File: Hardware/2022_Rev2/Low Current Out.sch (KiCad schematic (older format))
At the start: 72 parts

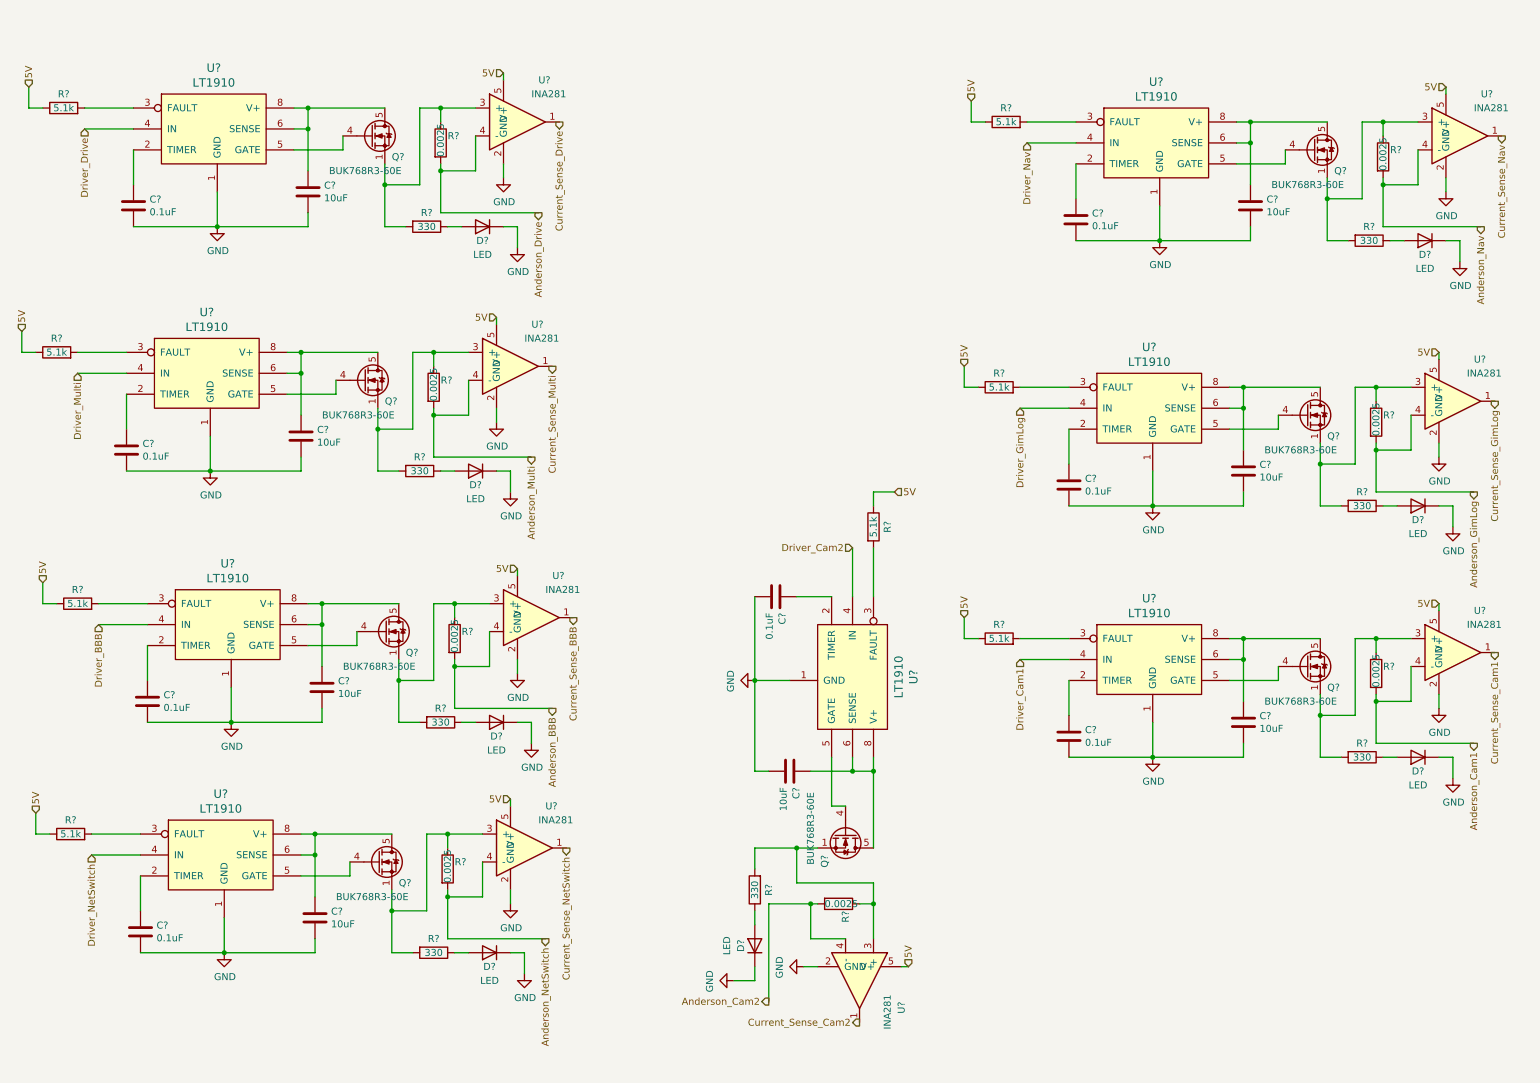
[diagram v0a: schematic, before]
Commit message: assigning footprints pt.1
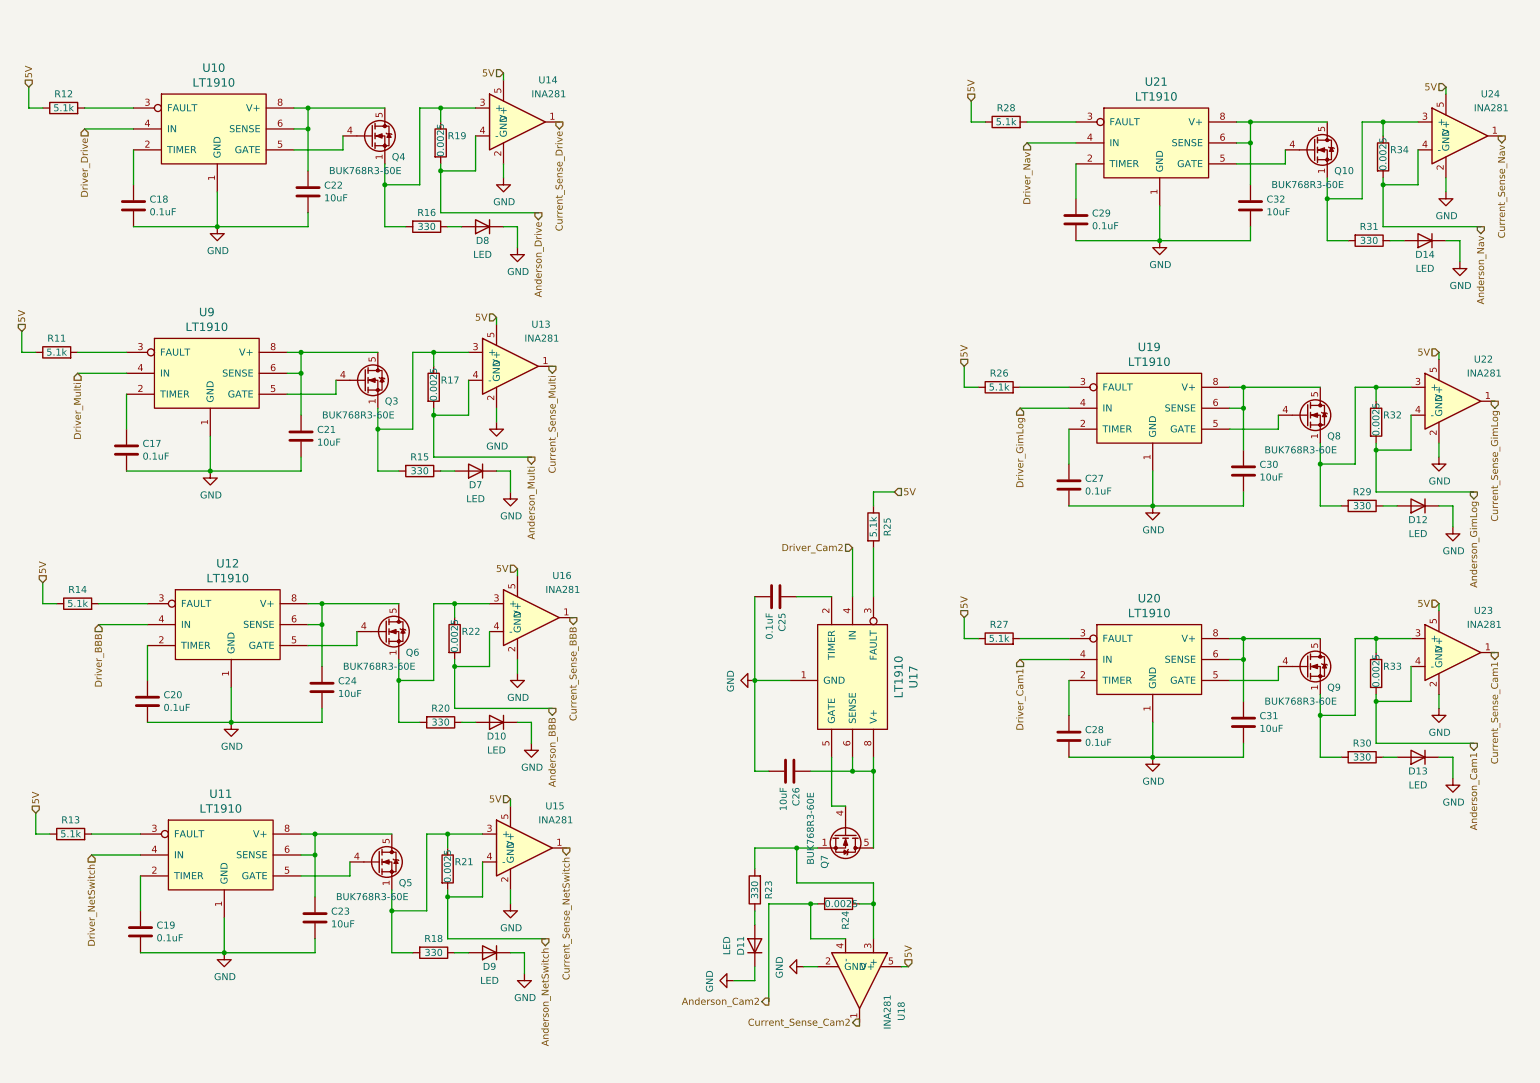
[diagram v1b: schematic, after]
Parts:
- C17, C18, C19, C20, C21, C22, C23, C24, C25, C26, C27, C28, C29, C30, C31, C32: renamed from C?; footprint (none) -> Capacitor_SMD:C_0603_1608Metric_Pad1.08x0.95mm_HandSolder
- D10, D11, D12, D13, D14, D7, D8, D9: renamed from D?; footprint (none) -> Diode_SMD:D_0603_1608Metric_Pad1.05x0.95mm_HandSolder
- gave numbers to parts that had none: 48

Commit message: Finished footprint signatures and started schematic
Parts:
- R11, R12, R13, R14, R15, R16, R18, R20, R23, R25, R26, R27, R28, R29, R30, R31: footprint (none) -> Resistor_SMD:R_0603_1608Metric_Pad0.98x0.95mm_HandSolder
- R17, R19, R21, R22, R24, R32, R33, R34: footprint (none) -> Resistor_SMD:R_2512_6332Metric_Pad1.40x3.35mm_HandSolder
- U10, U11, U12, U17, U19, U20, U21, U9: footprint (none) -> Package_SO:SOIC-8_3.9x4.9mm_P1.27mm
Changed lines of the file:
@@
 F 0 "R14" V 1000 4650 50  0000 C CNN
 F 1 "5.1k" V 900 4650 50  0000 C CNN
-F 2 "" V 830 4650 50  0001 C CNN
+F 2 "Resistor_SMD:R_0603_1608Metric_Pad0.98x0.95mm_HandSolder" V 830 4650 50  0001 C CNN
 F 3 "~" H 900 4650 50  0001 C CNN
 	1    900  4650
@@
 F 0 "U12" H 1975 5737 60  0000 C CNN
 F 1 "LT1910" H 1975 5631 60  0000 C CNN
-F 2 "" H 1600 5050 60  0001 C CNN
+F 2 "Package_SO:SOIC-8_3.9x4.9mm_P1.27mm" H 1600 5050 60  0001 C CNN
 F 3 "" H 1600 5050 60  0001 C CNN
 	1    1600 5050
@@
 F 0 "R20" V 3400 5500 50  0000 C CNN
 F 1 "330" V 3500 5500 50  0000 C CNN
-F 2 "" V 3430 5500 50  0001 C CNN
+F 2 "Resistor_SMD:R_0603_1608Metric_Pad0.98x0.95mm_HandSolder" V 3430 5500 50  0001 C CNN
 F 3 "~" H 3500 5500 50  0001 C CNN
 	1    3500 5500
@@
 F 0 "R22" H 3650 4950 50  0000 L CNN
 F 1 "0.0025" V 3600 4800 50  0000 L CNN
-F 2 "" V 3530 4900 50  0001 C CNN
+F 2 "Resistor_SMD:R_2512_6332Metric_Pad1.40x3.35mm_HandSolder" V 3530 4900 50  0001 C CNN
 F 3 "~" H 3600 4900 50  0001 C CNN
 	1    3600 4900
@@
 F 0 "R11" V 850 2850 50  0000 C CNN
 F 1 "5.1k" V 750 2850 50  0000 C CNN
-F 2 "" V 680 2850 50  0001 C CNN
+F 2 "Resistor_SMD:R_0603_1608Metric_Pad0.98x0.95mm_HandSolder" V 680 2850 50  0001 C CNN
 F 3 "~" H 750 2850 50  0001 C CNN
 	1    750  2850
@@
 F 0 "U9" H 1825 3937 60  0000 C CNN
 F 1 "LT1910" H 1825 3831 60  0000 C CNN
-F 2 "" H 1450 3250 60  0001 C CNN
+F 2 "Package_SO:SOIC-8_3.9x4.9mm_P1.27mm" H 1450 3250 60  0001 C CNN
 F 3 "" H 1450 3250 60  0001 C CNN
 	1    1450 3250
@@
 F 0 "R15" V 3250 3700 50  0000 C CNN
 F 1 "330" V 3350 3700 50  0000 C CNN
-F 2 "" V 3280 3700 50  0001 C CNN
+F 2 "Resistor_SMD:R_0603_1608Metric_Pad0.98x0.95mm_HandSolder" V 3280 3700 50  0001 C CNN
 F 3 "~" H 3350 3700 50  0001 C CNN
 	1    3350 3700
@@
 F 0 "R17" H 3500 3150 50  0000 L CNN
 F 1 "0.0025" V 3450 3000 50  0000 L CNN
-F 2 "" V 3380 3100 50  0001 C CNN
+F 2 "Resistor_SMD:R_2512_6332Metric_Pad1.40x3.35mm_HandSolder" V 3380 3100 50  0001 C CNN
 F 3 "~" H 3450 3100 50  0001 C CNN
 	1    3450 3100
@@
 F 0 "R12" V 900 1100 50  0000 C CNN
 F 1 "5.1k" V 800 1100 50  0000 C CNN
-F 2 "" V 730 1100 50  0001 C CNN
+F 2 "Resistor_SMD:R_0603_1608Metric_Pad0.98x0.95mm_HandSolder" V 730 1100 50  0001 C CNN
 F 3 "~" H 800 1100 50  0001 C CNN
 	1    800  1100
@@
 F 0 "U10" H 1875 2187 60  0000 C CNN
 F 1 "LT1910" H 1875 2081 60  0000 C CNN
-F 2 "" H 1500 1500 60  0001 C CNN
+F 2 "Package_SO:SOIC-8_3.9x4.9mm_P1.27mm" H 1500 1500 60  0001 C CNN
 F 3 "" H 1500 1500 60  0001 C CNN
 	1    1500 1500
@@
 F 0 "R16" V 3300 1950 50  0000 C CNN
 F 1 "330" V 3400 1950 50  0000 C CNN
-F 2 "" V 3330 1950 50  0001 C CNN
+F 2 "Resistor_SMD:R_0603_1608Metric_Pad0.98x0.95mm_HandSolder" V 3330 1950 50  0001 C CNN
 F 3 "~" H 3400 1950 50  0001 C CNN
 	1    3400 1950
@@
 F 0 "R19" H 3550 1400 50  0000 L CNN
 F 1 "0.0025" V 3500 1250 50  0000 L CNN
-F 2 "" V 3430 1350 50  0001 C CNN
+F 2 "Resistor_SMD:R_2512_6332Metric_Pad1.40x3.35mm_HandSolder" V 3430 1350 50  0001 C CNN
 F 3 "~" H 3500 1350 50  0001 C CNN
 	1    3500 1350
@@
 F 0 "R28" V 7650 1200 50  0000 C CNN
 F 1 "5.1k" V 7550 1200 50  0000 C CNN
-F 2 "" V 7480 1200 50  0001 C CNN
+F 2 "Resistor_SMD:R_0603_1608Metric_Pad0.98x0.95mm_HandSolder" V 7480 1200 50  0001 C CNN
 F 3 "~" H 7550 1200 50  0001 C CNN
 	1    7550 1200
@@
 F 0 "U21" H 8625 2287 60  0000 C CNN
 F 1 "LT1910" H 8625 2181 60  0000 C CNN
-F 2 "" H 8250 1600 60  0001 C CNN
+F 2 "Package_SO:SOIC-8_3.9x4.9mm_P1.27mm" H 8250 1600 60  0001 C CNN
 F 3 "" H 8250 1600 60  0001 C CNN
 	1    8250 1600
@@
 F 0 "R31" V 10050 2050 50  0000 C CNN
 F 1 "330" V 10150 2050 50  0000 C CNN
-F 2 "" V 10080 2050 50  0001 C CNN
+F 2 "Resistor_SMD:R_0603_1608Metric_Pad0.98x0.95mm_HandSolder" V 10080 2050 50  0001 C CNN
 F 3 "~" H 10150 2050 50  0001 C CNN
 	1    10150 2050
@@
 F 0 "R34" H 10300 1500 50  0000 L CNN
 F 1 "0.0025" V 10250 1350 50  0000 L CNN
-F 2 "" V 10180 1450 50  0001 C CNN
+F 2 "Resistor_SMD:R_2512_6332Metric_Pad1.40x3.35mm_HandSolder" V 10180 1450 50  0001 C CNN
 F 3 "~" H 10250 1450 50  0001 C CNN
 	1    10250 1450
@@
 F 0 "R26" V 7600 3100 50  0000 C CNN
 F 1 "5.1k" V 7500 3100 50  0000 C CNN
-F 2 "" V 7430 3100 50  0001 C CNN
+F 2 "Resistor_SMD:R_0603_1608Metric_Pad0.98x0.95mm_HandSolder" V 7430 3100 50  0001 C CNN
 F 3 "~" H 7500 3100 50  0001 C CNN
 	1    7500 3100
@@
 F 0 "U19" H 8575 4187 60  0000 C CNN
 F 1 "LT1910" H 8575 4081 60  0000 C CNN
-F 2 "" H 8200 3500 60  0001 C CNN
+F 2 "Package_SO:SOIC-8_3.9x4.9mm_P1.27mm" H 8200 3500 60  0001 C CNN
 F 3 "" H 8200 3500 60  0001 C CNN
 	1    8200 3500
@@
 F 0 "R29" V 10000 3950 50  0000 C CNN
 F 1 "330" V 10100 3950 50  0000 C CNN
-F 2 "" V 10030 3950 50  0001 C CNN
+F 2 "Resistor_SMD:R_0603_1608Metric_Pad0.98x0.95mm_HandSolder" V 10030 3950 50  0001 C CNN
 F 3 "~" H 10100 3950 50  0001 C CNN
 	1    10100 3950
@@
 F 0 "R32" H 10250 3400 50  0000 L CNN
 F 1 "0.0025" V 10200 3250 50  0000 L CNN
-F 2 "" V 10130 3350 50  0001 C CNN
+F 2 "Resistor_SMD:R_2512_6332Metric_Pad1.40x3.35mm_HandSolder" V 10130 3350 50  0001 C CNN
 F 3 "~" H 10200 3350 50  0001 C CNN
 	1    10200 3350
@@
 F 0 "R27" V 7600 4900 50  0000 C CNN
 F 1 "5.1k" V 7500 4900 50  0000 C CNN
-F 2 "" V 7430 4900 50  0001 C CNN
+F 2 "Resistor_SMD:R_0603_1608Metric_Pad0.98x0.95mm_HandSolder" V 7430 4900 50  0001 C CNN
 F 3 "~" H 7500 4900 50  0001 C CNN
 	1    7500 4900
@@
 F 0 "U20" H 8575 5987 60  0000 C CNN
 F 1 "LT1910" H 8575 5881 60  0000 C CNN
-F 2 "" H 8200 5300 60  0001 C CNN
+F 2 "Package_SO:SOIC-8_3.9x4.9mm_P1.27mm" H 8200 5300 60  0001 C CNN
 F 3 "" H 8200 5300 60  0001 C CNN
 	1    8200 5300
@@
 F 0 "R30" V 10000 5750 50  0000 C CNN
 F 1 "330" V 10100 5750 50  0000 C CNN
-F 2 "" V 10030 5750 50  0001 C CNN
+F 2 "Resistor_SMD:R_0603_1608Metric_Pad0.98x0.95mm_HandSolder" V 10030 5750 50  0001 C CNN
 F 3 "~" H 10100 5750 50  0001 C CNN
 	1    10100 5750
@@
 F 0 "R33" H 10250 5200 50  0000 L CNN
 F 1 "0.0025" V 10200 5050 50  0000 L CNN
-F 2 "" V 10130 5150 50  0001 C CNN
+F 2 "Resistor_SMD:R_2512_6332Metric_Pad1.40x3.35mm_HandSolder" V 10130 5150 50  0001 C CNN
 F 3 "~" H 10200 5150 50  0001 C CNN
 	1    10200 5150
@@
 F 0 "R13" V 950 6300 50  0000 C CNN
 F 1 "5.1k" V 850 6300 50  0000 C CNN
-F 2 "" V 780 6300 50  0001 C CNN
+F 2 "Resistor_SMD:R_0603_1608Metric_Pad0.98x0.95mm_HandSolder" V 780 6300 50  0001 C CNN
 F 3 "~" H 850 6300 50  0001 C CNN
 	1    850  6300
@@
 F 0 "U11" H 1925 7387 60  0000 C CNN
 F 1 "LT1910" H 1925 7281 60  0000 C CNN
-F 2 "" H 1550 6700 60  0001 C CNN
+F 2 "Package_SO:SOIC-8_3.9x4.9mm_P1.27mm" H 1550 6700 60  0001 C CNN
 F 3 "" H 1550 6700 60  0001 C CNN
 	1    1550 6700
@@
 F 0 "R18" V 3350 7150 50  0000 C CNN
 F 1 "330" V 3450 7150 50  0000 C CNN
-F 2 "" V 3380 7150 50  0001 C CNN
+F 2 "Resistor_SMD:R_0603_1608Metric_Pad0.98x0.95mm_HandSolder" V 3380 7150 50  0001 C CNN
 F 3 "~" H 3450 7150 50  0001 C CNN
 	1    3450 7150
@@
 F 0 "R21" H 3600 6600 50  0000 L CNN
 F 1 "0.0025" V 3550 6450 50  0000 L CNN
-F 2 "" V 3480 6550 50  0001 C CNN
+F 2 "Resistor_SMD:R_2512_6332Metric_Pad1.40x3.35mm_HandSolder" V 3480 6550 50  0001 C CNN
 F 3 "~" H 3550 6550 50  0001 C CNN
 	1    3550 6550
@@
 F 0 "R25" V 6700 4100 50  0000 C CNN
 F 1 "5.1k" V 6600 4100 50  0000 C CNN
-F 2 "" V 6530 4100 50  0001 C CNN
+F 2 "Resistor_SMD:R_0603_1608Metric_Pad0.98x0.95mm_HandSolder" V 6530 4100 50  0001 C CNN
 F 3 "~" H 6600 4100 50  0001 C CNN
 	1    6600 4100
@@
 F 0 "U17" H 6575 5487 60  0000 C CNN
 F 1 "LT1910" H 6575 5381 60  0000 C CNN
-F 2 "" H 6200 4800 60  0001 C CNN
+F 2 "Package_SO:SOIC-8_3.9x4.9mm_P1.27mm" H 6200 4800 60  0001 C CNN
 F 3 "" H 6200 4800 60  0001 C CNN
 	1    6200 4800
@@
 F 0 "R23" V 5650 6700 50  0000 C CNN
 F 1 "330" V 5750 6700 50  0000 C CNN
-F 2 "" V 5680 6700 50  0001 C CNN
+F 2 "Resistor_SMD:R_0603_1608Metric_Pad0.98x0.95mm_HandSolder" V 5680 6700 50  0001 C CNN
 F 3 "~" H 5750 6700 50  0001 C CNN
 	1    5750 6700
@@
 F 0 "R24" H 6400 6850 50  0000 L CNN
 F 1 "0.0025" V 6350 6700 50  0000 L CNN
-F 2 "" V 6280 6800 50  0001 C CNN
+F 2 "Resistor_SMD:R_2512_6332Metric_Pad1.40x3.35mm_HandSolder" V 6280 6800 50  0001 C CNN
 F 3 "~" H 6350 6800 50  0001 C CNN
 	1    6350 6800

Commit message: Lots of Changes
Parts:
- added C?: 0.1uF, Capacitor_SMD:C_0603_1608Metric_Pad1.08x0.95mm_HandSolder, symbol Device:C
- added C?: 10uF, Capacitor_SMD:C_0603_1608Metric_Pad1.08x0.95mm_HandSolder, symbol Device:C
- added D?: LED, Diode_SMD:D_0603_1608Metric_Pad1.05x0.95mm_HandSolder, symbol Device:D
- added F? (x4): 5A, symbol Device:Fuse
- added Q?: BUK768R3-60E, Package_TO_SOT_SMD:LFPAK33, symbol Transistor_FET:BUK7M9R9-60EX
- added R?: 5.1k, Resistor_SMD:R_0603_1608Metric_Pad0.98x0.95mm_HandSolder, symbol Device:R
- added R?: 330, Resistor_SMD:R_0603_1608Metric_Pad0.98x0.95mm_HandSolder, symbol Device:R
- added R?: 0.0025, Resistor_SMD:R_2512_6332Metric_Pad1.40x3.35mm_HandSolder, symbol Device:R
- added U?: LT1910, Package_SO:SOIC-8_3.9x4.9mm_P1.27mm, symbol 2022_Rev2-rescue:LT1910-MRDT_ICs
- added U?: INA281, Package_TO_SOT_SMD:SOT-23-5, symbol 2022_Rev2-rescue:INA281-MRDT_ICs
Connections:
- net 5V: now also R?.1, U?.5 (V+)
- net GND: now also C?.2, C?.2, D?.1 (K), U?.1 (GND), U?.2 (GND)
- net 12VA: now reaches C24.1, Q6.5 (D), U12.6 (SENSE), U12.8 (V+)
- net 12VA: now also C22.1, C32.1, Q10.5 (D), Q4.5 (D), U10.6 (SENSE), U10.8 (V+), U21.6 (SENSE), U21.8 (V+), C?.1, F?.1, F?.1, F?.1, F?.1, Q?.5 (D), U?.6 (SENSE), U?.8 (V+)
- net at C21.1, Q3.5 (D), U9.6 (SENSE)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: now also F?.2
- net at C30.1, Q8.5 (D), U19.6 (SENSE)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: now also F?.2
- net at C31.1, Q9.5 (D), U20.6 (SENSE)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: now also C26.1, Q7.5 (D), U17.6 (SENSE), U17.8 (V+), F?.2
- net at C23.1, Q5.5 (D), U11.6 (SENSE)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: now also F?.2
- net Anderson_GimLog renamed Anderson_Gim
- net Current_Sense_GimLog renamed Current_Sense_Gim
- net Driver_GimLog renamed Driver_Gim
- new net: R?.2, U?.3 (FAULT)
- new net: C?.1, U?.2 (TIMER)
- new net: Q?.4 (G), U?.5 (GATE)
- new net: Q?.1 (S), Q?.2 (S), Q?.3 (S), R?.1, R?.2, U?.3 (+)
- new net: D?.2 (A), R?.1
- new net Anderson_Spare: R?.2, U?.4 (-)
- new net Current_Sense_Spare: U?.1
- new net Driver_Spare: U?.4 (IN)

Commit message: Fixed schematic and fixed annotations
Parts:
- gave numbers to parts that had none: 13
- renumbered C17 to C14, C18 to C15, C19 to C16, C20 to C17, C21 to C18, C22 to C19, C23 to C20, C24 to C21, C25 to C23, C26 to C25, C27 to C26, C28 to C27, C29 to C28, C30 to C29, C31 to C30, C32 to C31, D11 to D10, D7 to D6, D8 to D7, D9 to D8, D10 to D9, Q9 to Q10, Q10 to Q11, Q7 to Q8, Q8 to Q9, R11 to R10, R12 to R11, R13 to R12, R14 to R13, R15 to R14, R16 to R15, R17 to R16, R18 to R17, R19 to R18, R20 to R19, R21 to R20, R22 to R21, R23 to R24, R24 to R26, R25 to R27, R26 to R28, R27 to R29, R28 to R30, R29 to R31, R30 to R32, R31 to R33, R32 to R34, R33 to R35, R34 to R36, U11 to U10, U12 to U11, U13 to U12, U14 to U13, U15 to U14, U16 to U15, U17 to U18, U18 to U19, U19 to U20, U20 to U21, U21 to U22, U22 to U23, U23 to U24, U24 to U25, U9 to U8, U10 to U9
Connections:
- net 12VA renamed +12VA
- net 5V renamed +5V

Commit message: Assigned footprints and finished changes on schem
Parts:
- F6, F7, F8, F9: footprint (none) -> MRDT_Passives:ATC_Fuse_Block
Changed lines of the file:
@@
 F 0 "F8" H 7560 4246 50  0000 L CNN
 F 1 "5A" H 7560 4155 50  0000 L CNN
-F 2 "" V 7430 4200 50  0001 C CNN
+F 2 "MRDT_Passives:ATC_Fuse_Block" V 7430 4200 50  0001 C CNN
 F 3 "~" H 7500 4200 50  0001 C CNN
 	1    7500 4200
@@
 F 0 "F6" H 2760 2646 50  0000 L CNN
 F 1 "5A" H 2760 2555 50  0000 L CNN
-F 2 "" V 2630 2600 50  0001 C CNN
+F 2 "MRDT_Passives:ATC_Fuse_Block" V 2630 2600 50  0001 C CNN
 F 3 "~" H 2700 2600 50  0001 C CNN
 	1    2700 2600
@@
 F 0 "F9" H 9460 2946 50  0000 L CNN
 F 1 "5A" H 9460 2855 50  0000 L CNN
-F 2 "" V 9330 2900 50  0001 C CNN
+F 2 "MRDT_Passives:ATC_Fuse_Block" V 9330 2900 50  0001 C CNN
 F 3 "~" H 9400 2900 50  0001 C CNN
 	1    9400 2900
@@
 F 0 "F7" H 2810 6146 50  0000 L CNN
 F 1 "5A" H 2810 6055 50  0000 L CNN
-F 2 "" V 2680 6100 50  0001 C CNN
+F 2 "MRDT_Passives:ATC_Fuse_Block" V 2680 6100 50  0001 C CNN
 F 3 "~" H 2750 6100 50  0001 C CNN
 	1    2750 6100

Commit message: Fixed many issues
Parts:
- removed C16: 0.1uF, Capacitor_SMD:C_0603_1608Metric_Pad1.08x0.95mm_HandSolder, symbol Device:C
- removed C20: 10uF, Capacitor_SMD:C_0603_1608Metric_Pad1.08x0.95mm_HandSolder, symbol Device:C
- removed F7: 5A, MRDT_Passives:ATC_Fuse_Block, symbol Device:Fuse
- removed Q5: BUK768R3-60E, Package_TO_SOT_SMD:LFPAK33, symbol Transistor_FET:BUK7M9R9-60EX
- removed R12: 5.1k, Resistor_SMD:R_0603_1608Metric_Pad0.98x0.95mm_HandSolder, symbol Device:R
- removed R20: 0.0025, Resistor_SMD:R_2512_6332Metric_Pad1.40x3.35mm_HandSolder, symbol Device:R
- removed U10: LT1910, Package_SO:SOIC-8_3.9x4.9mm_P1.27mm, symbol 2022_Rev2-rescue:LT1910-MRDT_ICs
- removed U14: INA281, Package_TO_SOT_SMD:SOT-23-5, symbol 2022_Rev2-rescue:INA281-MRDT_ICs
- R14, R15, R17, R19, R24, R25, R31, R32, R33: value 330 -> 1k
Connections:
- net +12VA: now also R17.2
